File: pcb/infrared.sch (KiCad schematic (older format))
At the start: 15 parts, among them U3 QRE1113GR, U4 QRE1113GR, U5 QRE1113GR, U6 QRE1113GR, U7 QRE1113GR, U8 QRE1113GR, U9 QRE1113GR

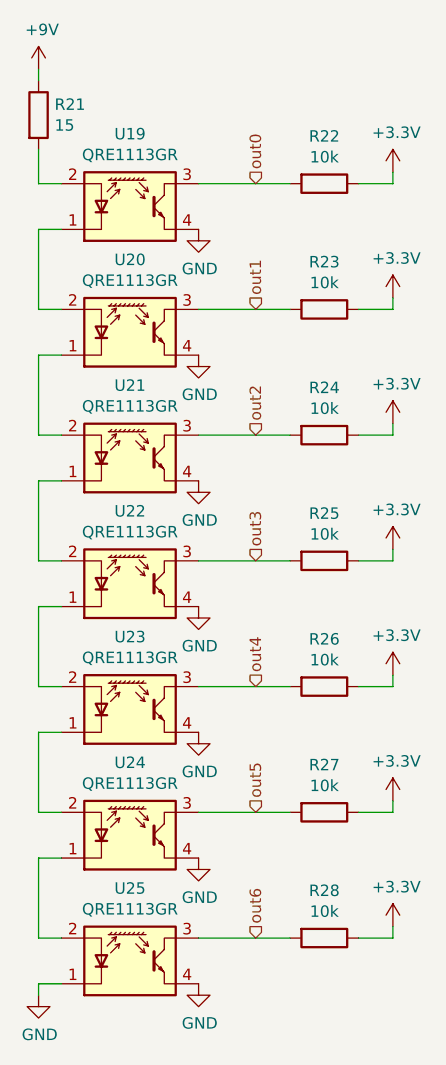
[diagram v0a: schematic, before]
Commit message: Infrared index starts at 0
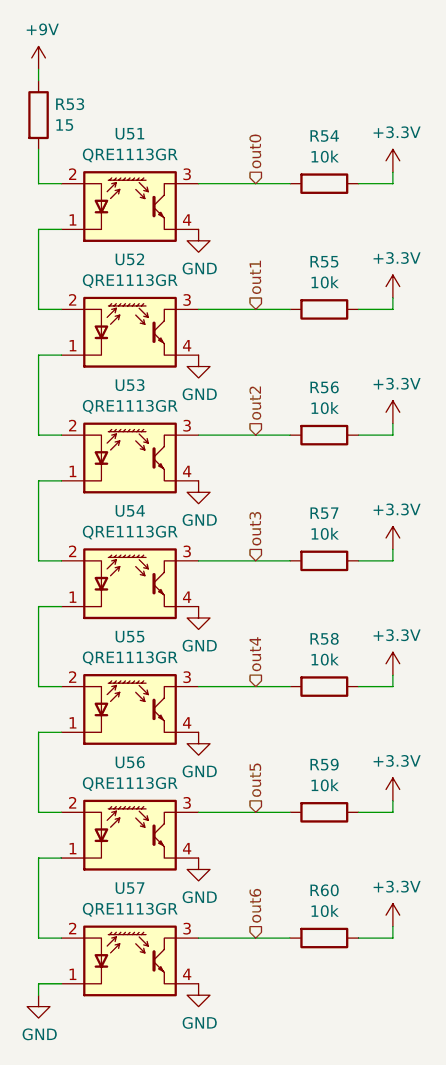
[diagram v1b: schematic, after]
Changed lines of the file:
@@
 $Descr A4 11693 8268
 encoding utf-8
-Sheet 9 17
+Sheet 11 17
 Title ""
 Date ""
@@
 AR Path="/5D1373A3/5D2E89D4/5D2FCBFF/5D171D8B" Ref="U?"  Part="1"
 AR Path="/5D1373A3/5D2E8A06/5D2FCBFF/5D171D8B" Ref="U?"  Part="1"
-F 0 "U25" H 5500 5817 50  0000 C CNN
+F 0 "U57" H 5500 5817 50  0000 C CNN
 F 1 "QRE1113GR" H 5500 5726 50  0000 C CNN
 F 2 "OptoDevice:OnSemi_CASE100CY" H 5500 5300 50  0001 C CNN
@@
 AR Path="/5D1373A3/5D2E89D4/5D2FCBFF/5D178379" Ref="#PWR?"  Part="1"
 AR Path="/5D1373A3/5D2E8A06/5D2FCBFF/5D178379" Ref="#PWR?"  Part="1"
-F 0 "#PWR075" H 5100 5400 50  0001 C CNN
+F 0 "#PWR0151" H 5100 5400 50  0001 C CNN
 F 1 "GND" H 5105 5477 50  0000 C CNN
 F 2 "" H 5100 5650 50  0001 C CNN
@@
 AR Path="/5D1373A3/5D2E89D4/5D2FCBFF/5D17EBA8" Ref="U?"  Part="1"
 AR Path="/5D1373A3/5D2E8A06/5D2FCBFF/5D17EBA8" Ref="U?"  Part="1"
-F 0 "U24" H 5500 5267 50  0000 C CNN
+F 0 "U56" H 5500 5267 50  0000 C CNN
 F 1 "QRE1113GR" H 5500 5176 50  0000 C CNN
 F 2 "OptoDevice:OnSemi_CASE100CY" H 5500 4750 50  0001 C CNN
@@
 AR Path="/5D1373A3/5D2E89D4/5D2FCBFF/5D17F20E" Ref="U?"  Part="1"
 AR Path="/5D1373A3/5D2E8A06/5D2FCBFF/5D17F20E" Ref="U?"  Part="1"
-F 0 "U23" H 5500 4717 50  0000 C CNN
+F 0 "U55" H 5500 4717 50  0000 C CNN
 F 1 "QRE1113GR" H 5500 4626 50  0000 C CNN
 F 2 "OptoDevice:OnSemi_CASE100CY" H 5500 4200 50  0001 C CNN
@@
 AR Path="/5D1373A3/5D2E89D4/5D2FCBFF/5D17FB11" Ref="U?"  Part="1"
 AR Path="/5D1373A3/5D2E8A06/5D2FCBFF/5D17FB11" Ref="U?"  Part="1"
-F 0 "U22" H 5500 4167 50  0000 C CNN
+F 0 "U54" H 5500 4167 50  0000 C CNN
 F 1 "QRE1113GR" H 5500 4076 50  0000 C CNN
 F 2 "OptoDevice:OnSemi_CASE100CY" H 5500 3650 50  0001 C CNN
@@
 AR Path="/5D1373A3/5D2E89D4/5D2FCBFF/5D187B41" Ref="U?"  Part="1"
 AR Path="/5D1373A3/5D2E8A06/5D2FCBFF/5D187B41" Ref="U?"  Part="1"
-F 0 "U21" H 5500 3617 50  0000 C CNN
+F 0 "U53" H 5500 3617 50  0000 C CNN
 F 1 "QRE1113GR" H 5500 3526 50  0000 C CNN
 F 2 "OptoDevice:OnSemi_CASE100CY" H 5500 3100 50  0001 C CNN
@@
 AR Path="/5D1373A3/5D2E89D4/5D2FCBFF/5D195F28" Ref="U?"  Part="1"
 AR Path="/5D1373A3/5D2E8A06/5D2FCBFF/5D195F28" Ref="U?"  Part="1"
-F 0 "U20" H 5500 3067 50  0000 C CNN
+F 0 "U52" H 5500 3067 50  0000 C CNN
 F 1 "QRE1113GR" H 5500 2976 50  0000 C CNN
 F 2 "OptoDevice:OnSemi_CASE100CY" H 5500 2550 50  0001 C CNN
@@
 AR Path="/5D1373A3/5D2E89D4/5D2FCBFF/5D1A6C4E" Ref="#PWR?"  Part="1"
 AR Path="/5D1373A3/5D2E8A06/5D2FCBFF/5D1A6C4E" Ref="#PWR?"  Part="1"
-F 0 "#PWR062" H 5800 2050 50  0001 C CNN
+F 0 "#PWR0138" H 5800 2050 50  0001 C CNN
 F 1 "GND" H 5805 2127 50  0000 C CNN
 F 2 "" H 5800 2300 50  0001 C CNN
@@
 AR Path="/5D1373A3/5D2E89D4/5D2FCBFF/5D1A4E04" Ref="#PWR?"  Part="1"
 AR Path="/5D1373A3/5D2E8A06/5D2FCBFF/5D1A4E04" Ref="#PWR?"  Part="1"
-F 0 "#PWR061" H 6650 1900 50  0001 C CNN
+F 0 "#PWR0137" H 6650 1900 50  0001 C CNN
 F 1 "+3.3V" H 6665 2223 50  0000 C CNN
 F 2 "" H 6650 2050 50  0001 C CNN
@@
 AR Path="/5D1373A3/5D2E89D4/5D2FCBFF/5D196DB3" Ref="U?"  Part="1"
 AR Path="/5D1373A3/5D2E8A06/5D2FCBFF/5D196DB3" Ref="U?"  Part="1"
-F 0 "U19" H 5500 2517 50  0000 C CNN
+F 0 "U51" H 5500 2517 50  0000 C CNN
 F 1 "QRE1113GR" H 5500 2426 50  0000 C CNN
 F 2 "OptoDevice:OnSemi_CASE100CY" H 5500 2000 50  0001 C CNN
@@
 AR Path="/5D1373A3/5D2E89D4/5D2FCBFF/5D17A439" Ref="#PWR?"  Part="1"
 AR Path="/5D1373A3/5D2E8A06/5D2FCBFF/5D17A439" Ref="#PWR?"  Part="1"
-F 0 "#PWR060" H 5100 1450 50  0001 C CNN
+F 0 "#PWR0136" H 5100 1450 50  0001 C CNN
 F 1 "+9V" H 5115 1773 50  0000 C CNN
 F 2 "" H 5100 1600 50  0001 C CNN
@@
 AR Path="/5D1373A3/5D2E89D4/5D2FCBFF/5D175061" Ref="R?"  Part="1"
 AR Path="/5D1373A3/5D2E8A06/5D2FCBFF/5D175061" Ref="R?"  Part="1"
-F 0 "R21" H 5170 1846 50  0000 L CNN
+F 0 "R53" H 5170 1846 50  0000 L CNN
 F 1 "15" H 5170 1755 50  0000 L CNN
 F 2 "Resistor_SMD:R_0805_2012Metric" V 5030 1800 50  0001 C CNN
@@
 AR Path="/5D1373A3/5D2E89D4/5D2FCBFF/5D1C87B0" Ref="R?"  Part="1"
 AR Path="/5D1373A3/5D2E8A06/5D2FCBFF/5D1C87B0" Ref="R?"  Part="1"
-F 0 "R22" V 6143 2100 50  0000 C CNN
+F 0 "R54" V 6143 2100 50  0000 C CNN
 F 1 "10k" V 6234 2100 50  0000 C CNN
 F 2 "Resistor_SMD:R_0805_2012Metric" V 6280 2100 50  0001 C CNN
@@
 AR Path="/5D1373A3/5D2E89D4/5D2FCBFF/5D1CFAC7" Ref="#PWR?"  Part="1"
 AR Path="/5D1373A3/5D2E8A06/5D2FCBFF/5D1CFAC7" Ref="#PWR?"  Part="1"
-F 0 "#PWR063" H 6650 2450 50  0001 C CNN
+F 0 "#PWR0139" H 6650 2450 50  0001 C CNN
 F 1 "+3.3V" H 6665 2773 50  0000 C CNN
 F 2 "" H 6650 2600 50  0001 C CNN
@@
 AR Path="/5D1373A3/5D2E89D4/5D2FCBFF/5D1CFACE" Ref="R?"  Part="1"
 AR Path="/5D1373A3/5D2E8A06/5D2FCBFF/5D1CFACE" Ref="R?"  Part="1"
-F 0 "R23" V 6143 2650 50  0000 C CNN
+F 0 "R55" V 6143 2650 50  0000 C CNN
 F 1 "10k" V 6234 2650 50  0000 C CNN
 F 2 "Resistor_SMD:R_0805_2012Metric" V 6280 2650 50  0001 C CNN
@@
 AR Path="/5D1373A3/5D2E89D4/5D2FCBFF/5D1D407E" Ref="#PWR?"  Part="1"
 AR Path="/5D1373A3/5D2E8A06/5D2FCBFF/5D1D407E" Ref="#PWR?"  Part="1"
-F 0 "#PWR065" H 6650 3000 50  0001 C CNN
+F 0 "#PWR0141" H 6650 3000 50  0001 C CNN
 F 1 "+3.3V" H 6665 3323 50  0000 C CNN
 F 2 "" H 6650 3150 50  0001 C CNN
@@
 AR Path="/5D1373A3/5D2E89D4/5D2FCBFF/5D1D4085" Ref="R?"  Part="1"
 AR Path="/5D1373A3/5D2E8A06/5D2FCBFF/5D1D4085" Ref="R?"  Part="1"
-F 0 "R24" V 6143 3200 50  0000 C CNN
+F 0 "R56" V 6143 3200 50  0000 C CNN
 F 1 "10k" V 6234 3200 50  0000 C CNN
 F 2 "Resistor_SMD:R_0805_2012Metric" V 6280 3200 50  0001 C CNN
@@
 AR Path="/5D1373A3/5D2E89D4/5D2FCBFF/5D1D5122" Ref="#PWR?"  Part="1"
 AR Path="/5D1373A3/5D2E8A06/5D2FCBFF/5D1D5122" Ref="#PWR?"  Part="1"
-F 0 "#PWR067" H 6650 3550 50  0001 C CNN
+F 0 "#PWR0143" H 6650 3550 50  0001 C CNN
 F 1 "+3.3V" H 6665 3873 50  0000 C CNN
 F 2 "" H 6650 3700 50  0001 C CNN
@@
 AR Path="/5D1373A3/5D2E89D4/5D2FCBFF/5D1D5129" Ref="R?"  Part="1"
 AR Path="/5D1373A3/5D2E8A06/5D2FCBFF/5D1D5129" Ref="R?"  Part="1"
-F 0 "R25" V 6143 3750 50  0000 C CNN
+F 0 "R57" V 6143 3750 50  0000 C CNN
 F 1 "10k" V 6234 3750 50  0000 C CNN
 F 2 "Resistor_SMD:R_0805_2012Metric" V 6280 3750 50  0001 C CNN
@@
 AR Path="/5D1373A3/5D2E89D4/5D2FCBFF/5D1D6160" Ref="#PWR?"  Part="1"
 AR Path="/5D1373A3/5D2E8A06/5D2FCBFF/5D1D6160" Ref="#PWR?"  Part="1"
-F 0 "#PWR069" H 6650 4100 50  0001 C CNN
+F 0 "#PWR0145" H 6650 4100 50  0001 C CNN
 F 1 "+3.3V" H 6665 4423 50  0000 C CNN
 F 2 "" H 6650 4250 50  0001 C CNN
@@
 AR Path="/5D1373A3/5D2E89D4/5D2FCBFF/5D1D6167" Ref="R?"  Part="1"
 AR Path="/5D1373A3/5D2E8A06/5D2FCBFF/5D1D6167" Ref="R?"  Part="1"
-F 0 "R26" V 6143 4300 50  0000 C CNN
+F 0 "R58" V 6143 4300 50  0000 C CNN
 F 1 "10k" V 6234 4300 50  0000 C CNN
 F 2 "Resistor_SMD:R_0805_2012Metric" V 6280 4300 50  0001 C CNN
@@
 AR Path="/5D1373A3/5D2E89D4/5D2FCBFF/5D1D71C5" Ref="#PWR?"  Part="1"
 AR Path="/5D1373A3/5D2E8A06/5D2FCBFF/5D1D71C5" Ref="#PWR?"  Part="1"
-F 0 "#PWR071" H 6650 4650 50  0001 C CNN
+F 0 "#PWR0147" H 6650 4650 50  0001 C CNN
 F 1 "+3.3V" H 6665 4973 50  0000 C CNN
 F 2 "" H 6650 4800 50  0001 C CNN
@@
 AR Path="/5D1373A3/5D2E89D4/5D2FCBFF/5D1D71CC" Ref="R?"  Part="1"
 AR Path="/5D1373A3/5D2E8A06/5D2FCBFF/5D1D71CC" Ref="R?"  Part="1"
-F 0 "R27" V 6143 4850 50  0000 C CNN
+F 0 "R59" V 6143 4850 50  0000 C CNN
 F 1 "10k" V 6234 4850 50  0000 C CNN
 F 2 "Resistor_SMD:R_0805_2012Metric" V 6280 4850 50  0001 C CNN
@@
 AR Path="/5D1373A3/5D2E89D4/5D2FCBFF/5D1D9258" Ref="#PWR?"  Part="1"
 AR Path="/5D1373A3/5D2E8A06/5D2FCBFF/5D1D9258" Ref="#PWR?"  Part="1"
-F 0 "#PWR073" H 6650 5200 50  0001 C CNN
+F 0 "#PWR0149" H 6650 5200 50  0001 C CNN
 F 1 "+3.3V" H 6665 5523 50  0000 C CNN
 F 2 "" H 6650 5350 50  0001 C CNN
@@
 AR Path="/5D1373A3/5D2E89D4/5D2FCBFF/5D1D925F" Ref="R?"  Part="1"
 AR Path="/5D1373A3/5D2E8A06/5D2FCBFF/5D1D925F" Ref="R?"  Part="1"
-F 0 "R28" V 6143 5400 50  0000 C CNN
+F 0 "R60" V 6143 5400 50  0000 C CNN
 F 1 "10k" V 6234 5400 50  0000 C CNN
 F 2 "Resistor_SMD:R_0805_2012Metric" V 6280 5400 50  0001 C CNN
@@
 AR Path="/5D1373A3/5D2E89D4/5D2FCBFF/5D1D9CCE" Ref="#PWR?"  Part="1"
 AR Path="/5D1373A3/5D2E8A06/5D2FCBFF/5D1D9CCE" Ref="#PWR?"  Part="1"
-F 0 "#PWR064" H 5800 2600 50  0001 C CNN
+F 0 "#PWR0140" H 5800 2600 50  0001 C CNN
 F 1 "GND" H 5805 2677 50  0000 C CNN
 F 2 "" H 5800 2850 50  0001 C CNN
@@
 AR Path="/5D1373A3/5D2E89D4/5D2FCBFF/5D1DA3A9" Ref="#PWR?"  Part="1"
 AR Path="/5D1373A3/5D2E8A06/5D2FCBFF/5D1DA3A9" Ref="#PWR?"  Part="1"
-F 0 "#PWR066" H 5800 3150 50  0001 C CNN
+F 0 "#PWR0142" H 5800 3150 50  0001 C CNN
 F 1 "GND" H 5805 3227 50  0000 C CNN
 F 2 "" H 5800 3400 50  0001 C CNN
@@
 AR Path="/5D1373A3/5D2E89D4/5D2FCBFF/5D1DA8FE" Ref="#PWR?"  Part="1"
 AR Path="/5D1373A3/5D2E8A06/5D2FCBFF/5D1DA8FE" Ref="#PWR?"  Part="1"
-F 0 "#PWR068" H 5800 3700 50  0001 C CNN
+F 0 "#PWR0144" H 5800 3700 50  0001 C CNN
 F 1 "GND" H 5805 3777 50  0000 C CNN
 F 2 "" H 5800 3950 50  0001 C CNN
@@
 AR Path="/5D1373A3/5D2E89D4/5D2FCBFF/5D1DAF50" Ref="#PWR?"  Part="1"
 AR Path="/5D1373A3/5D2E8A06/5D2FCBFF/5D1DAF50" Ref="#PWR?"  Part="1"
-F 0 "#PWR070" H 5800 4250 50  0001 C CNN
+F 0 "#PWR0146" H 5800 4250 50  0001 C CNN
 F 1 "GND" H 5805 4327 50  0000 C CNN
 F 2 "" H 5800 4500 50  0001 C CNN
@@
 AR Path="/5D1373A3/5D2E89D4/5D2FCBFF/5D1DB5E7" Ref="#PWR?"  Part="1"
 AR Path="/5D1373A3/5D2E8A06/5D2FCBFF/5D1DB5E7" Ref="#PWR?"  Part="1"
-F 0 "#PWR072" H 5800 4800 50  0001 C CNN
+F 0 "#PWR0148" H 5800 4800 50  0001 C CNN
 F 1 "GND" H 5805 4877 50  0000 C CNN
 F 2 "" H 5800 5050 50  0001 C CNN
@@
 AR Path="/5D1373A3/5D2E89D4/5D2FCBFF/5D1DBD43" Ref="#PWR?"  Part="1"
 AR Path="/5D1373A3/5D2E8A06/5D2FCBFF/5D1DBD43" Ref="#PWR?"  Part="1"
-F 0 "#PWR074" H 5800 5350 50  0001 C CNN
+F 0 "#PWR0150" H 5800 5350 50  0001 C CNN
 F 1 "GND" H 5805 5427 50  0000 C CNN
 F 2 "" H 5800 5600 50  0001 C CNN
